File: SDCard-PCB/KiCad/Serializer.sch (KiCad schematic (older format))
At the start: 32 parts, among them J1 Conn_01x01, U8 DS90UB933-Q1

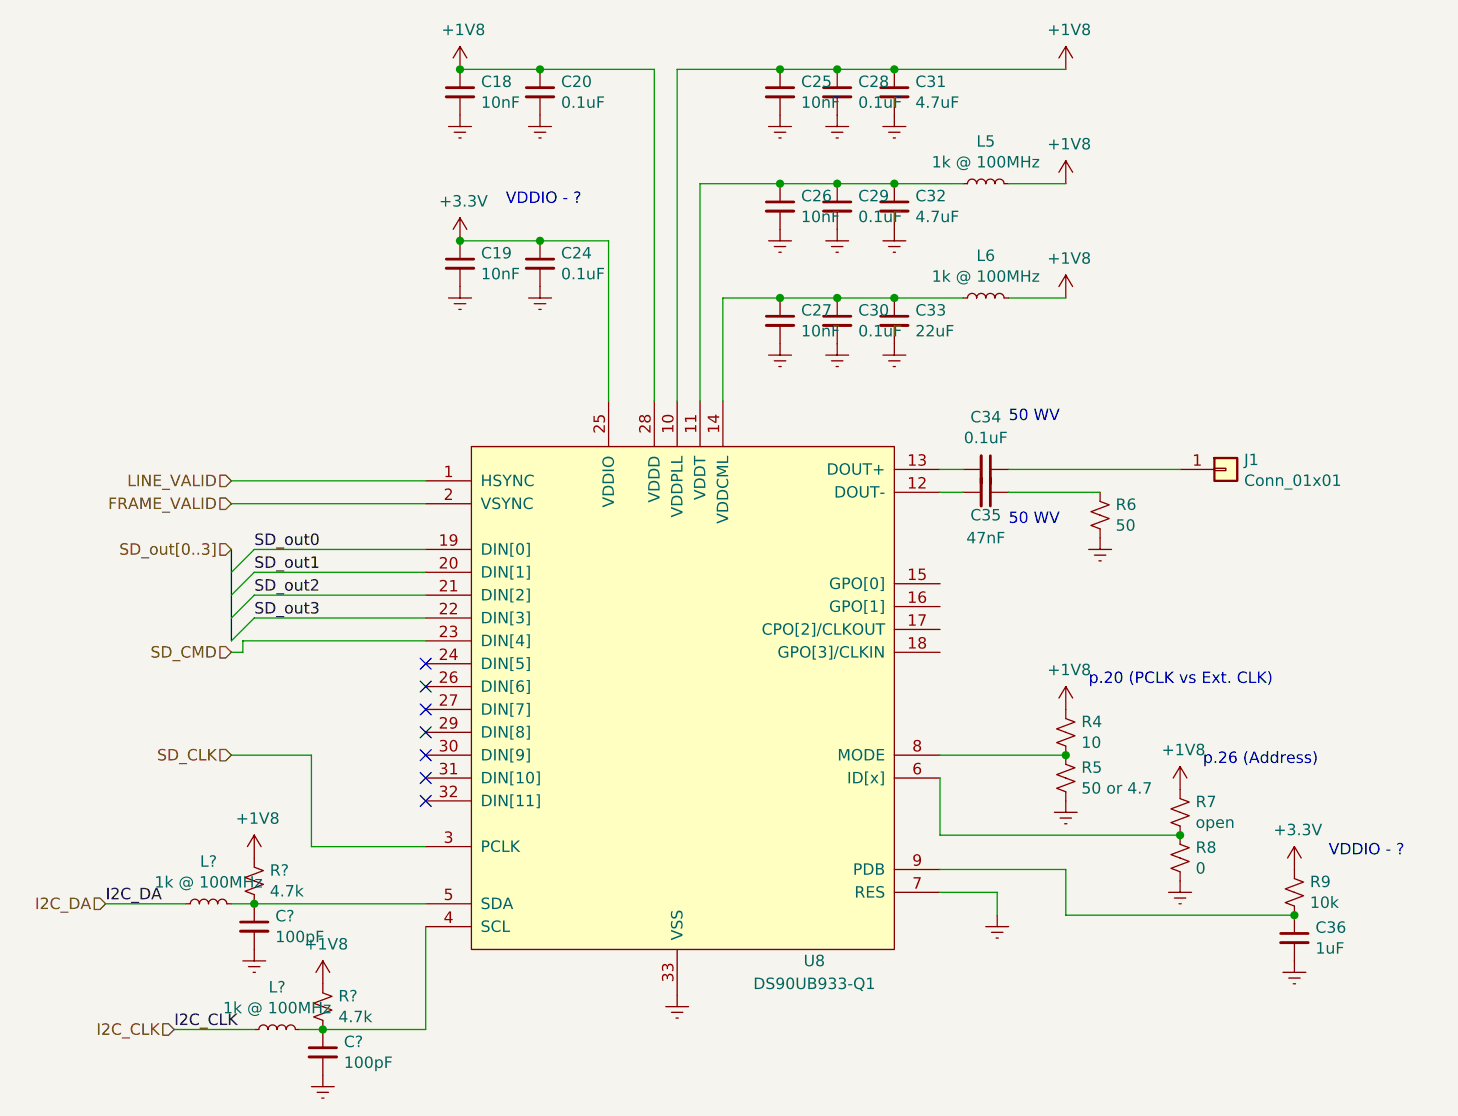
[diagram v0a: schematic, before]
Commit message: Finish schematics, begin PCB design
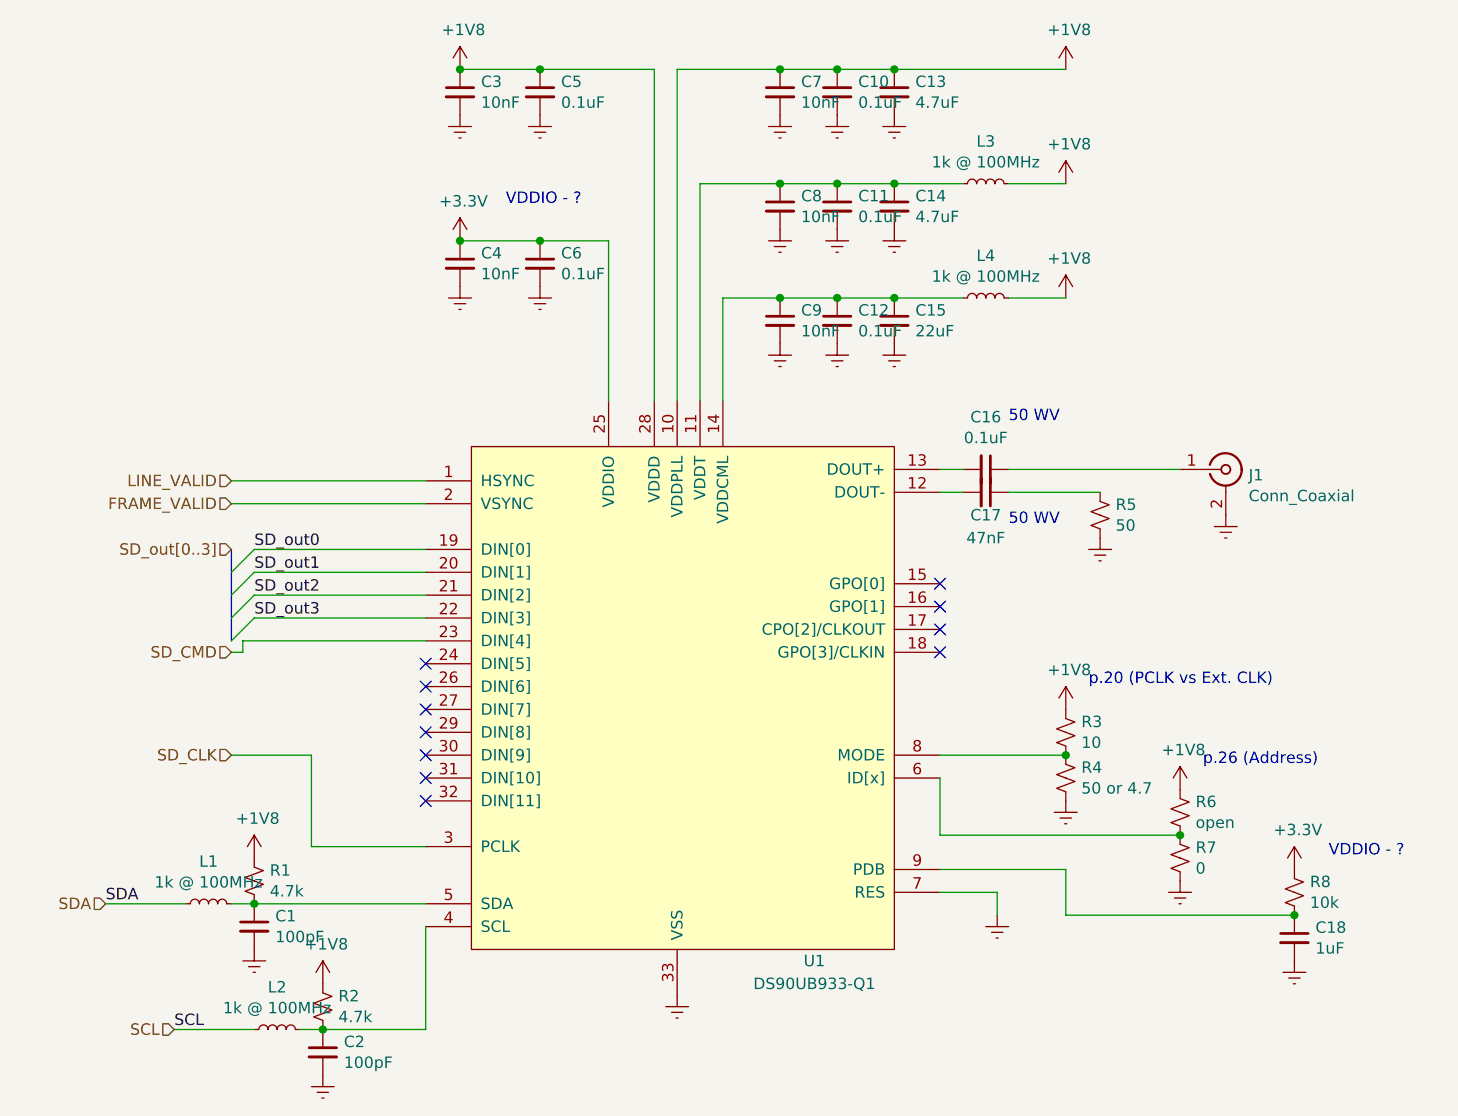
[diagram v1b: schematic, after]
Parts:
- removed J1: Conn_01x01, symbol .Connector:Conn_01x01
- added J1: Conn_Coaxial, .Connector:SMA-J-P-H-RA-TH1, symbol Connector:Conn_Coaxial
- L1, L2: renamed from L?; footprint (none) -> .Inductor:L_0603_1608Metric_L
- L3: renamed from L5; footprint (none) -> .Inductor:L_0603_1608Metric_L
- L4: renamed from L6; footprint (none) -> .Inductor:L_0603_1608Metric_L
- R1, R2: renamed from R?; footprint (none) -> .Resistor:R_0402_1005Metric_ERJ_L
- R3: renamed from R4; footprint (none) -> .Resistor:R_0402_1005Metric_ERJ_L
- R4: renamed from R5; footprint (none) -> .Resistor:R_0402_1005Metric_ERJ_L
- R5: renamed from R6; footprint (none) -> .Resistor:R_0402_1005Metric_ERJ_L
- R6: renamed from R7; footprint (none) -> .Resistor:R_0402_1005Metric_ERJ_L
- R7: renamed from R8; footprint (none) -> .Resistor:R_0402_1005Metric_ERJ_L
- R8: renamed from R9; footprint (none) -> .Resistor:R_0402_1005Metric_ERJ_L
- gave numbers to parts that had none: 2
- renumbered C28 to C10, C29 to C11, C30 to C12, C31 to C13, C32 to C14, C33 to C15, C34 to C16, C35 to C17, C36 to C18, C18 to C3, C19 to C4, C20 to C5, C24 to C6, C25 to C7, C26 to C8, C27 to C9, U8 to U1
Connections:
- net Earth: now also J1.2 (Ext)
- net at C16.1: now also J1.1 (In)
- net I2C_CLK renamed SCL
- net I2C_DA renamed SDA
- no-connect marks 7 -> 11
